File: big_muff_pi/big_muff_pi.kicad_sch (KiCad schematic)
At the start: 77 parts, among them J1 Jack_6.35, J2 Jack_6.35, J3 Conn_01x05, J4 Conn_01x05, J5 Conn_01x05, J7 Conn_01x01_Socket, J8 Conn_01x01_Socket, J9 Barrel_Jack_Switch, P1 big_muff_pi_front_panel, Q1 MMBT5551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

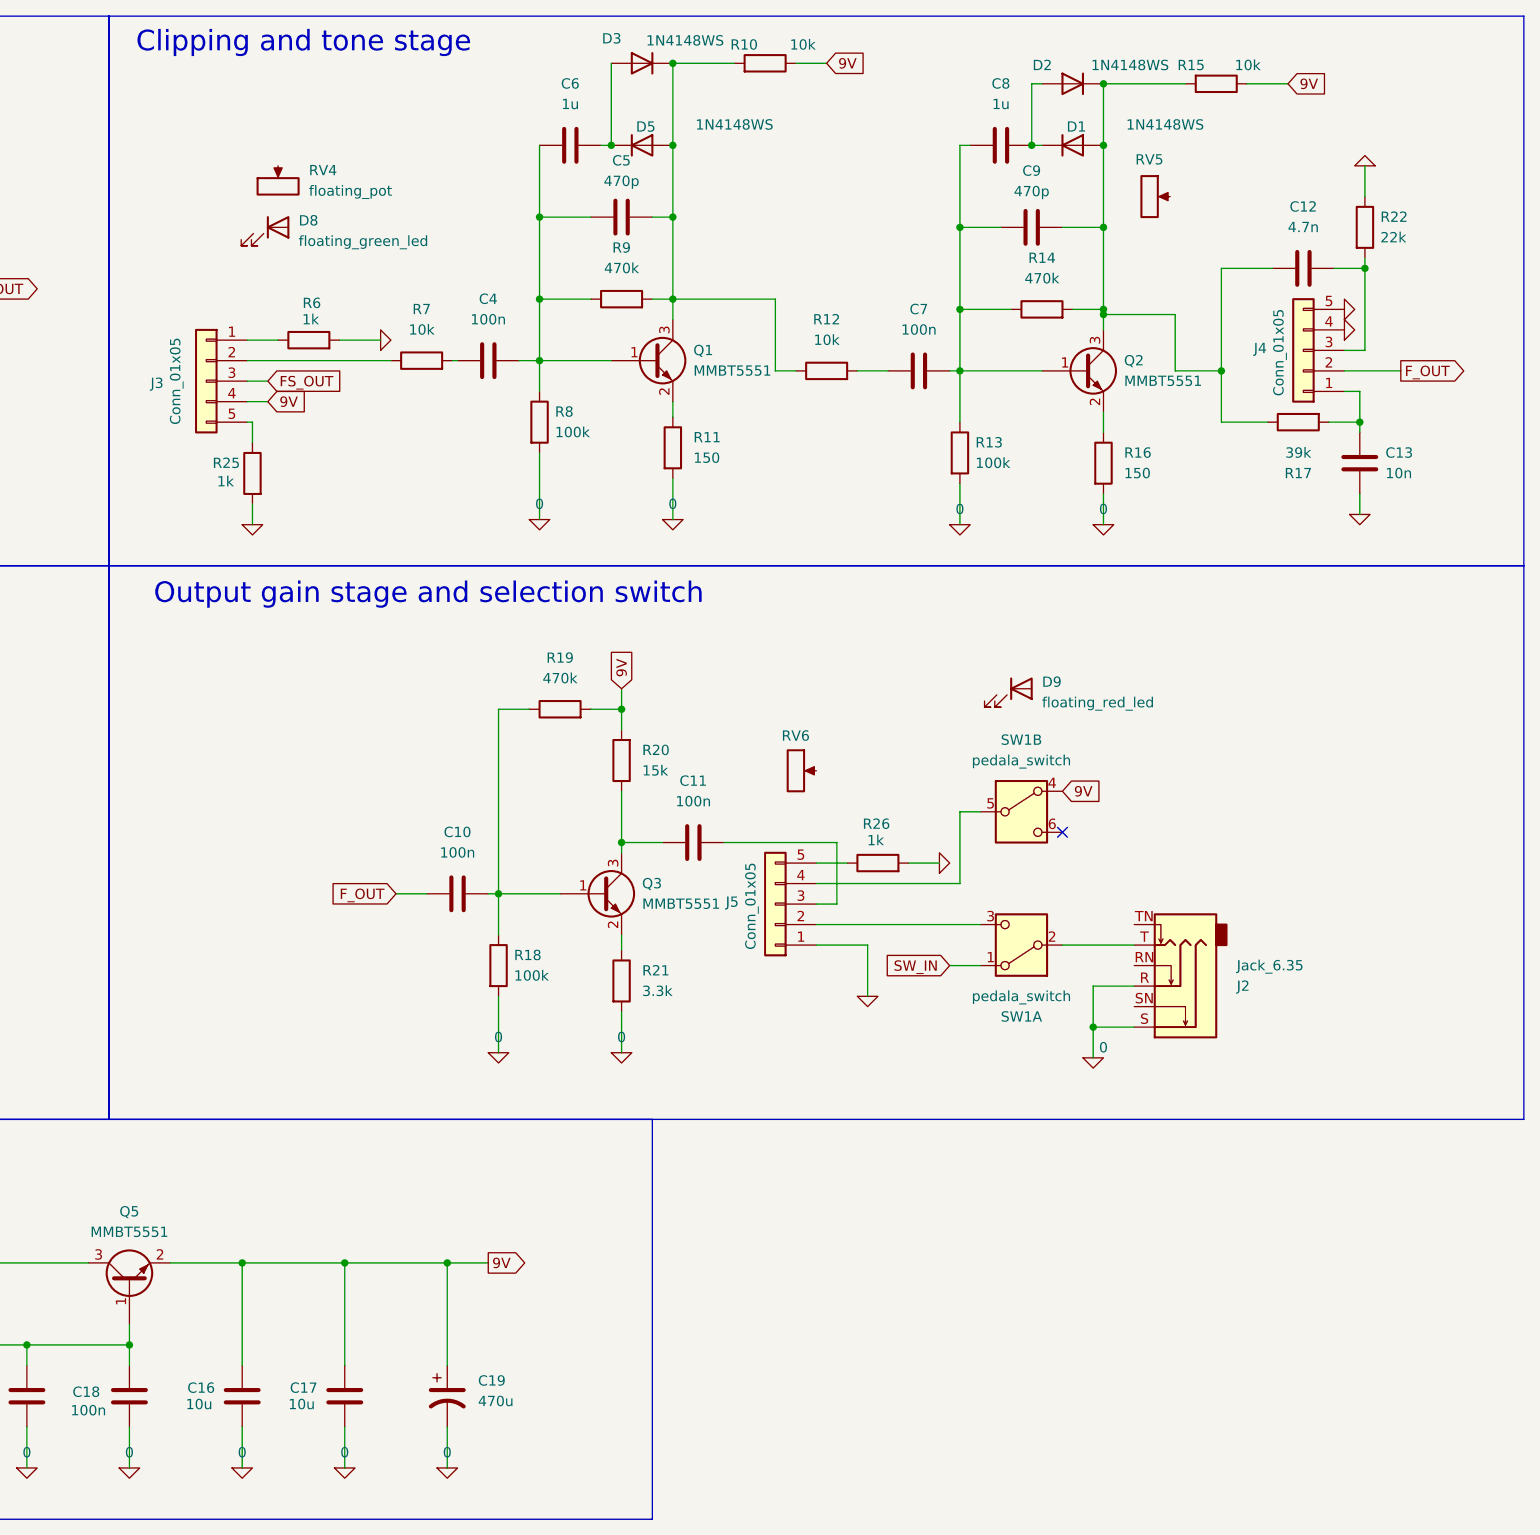
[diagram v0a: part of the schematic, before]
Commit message: Added IDC, added front plate.
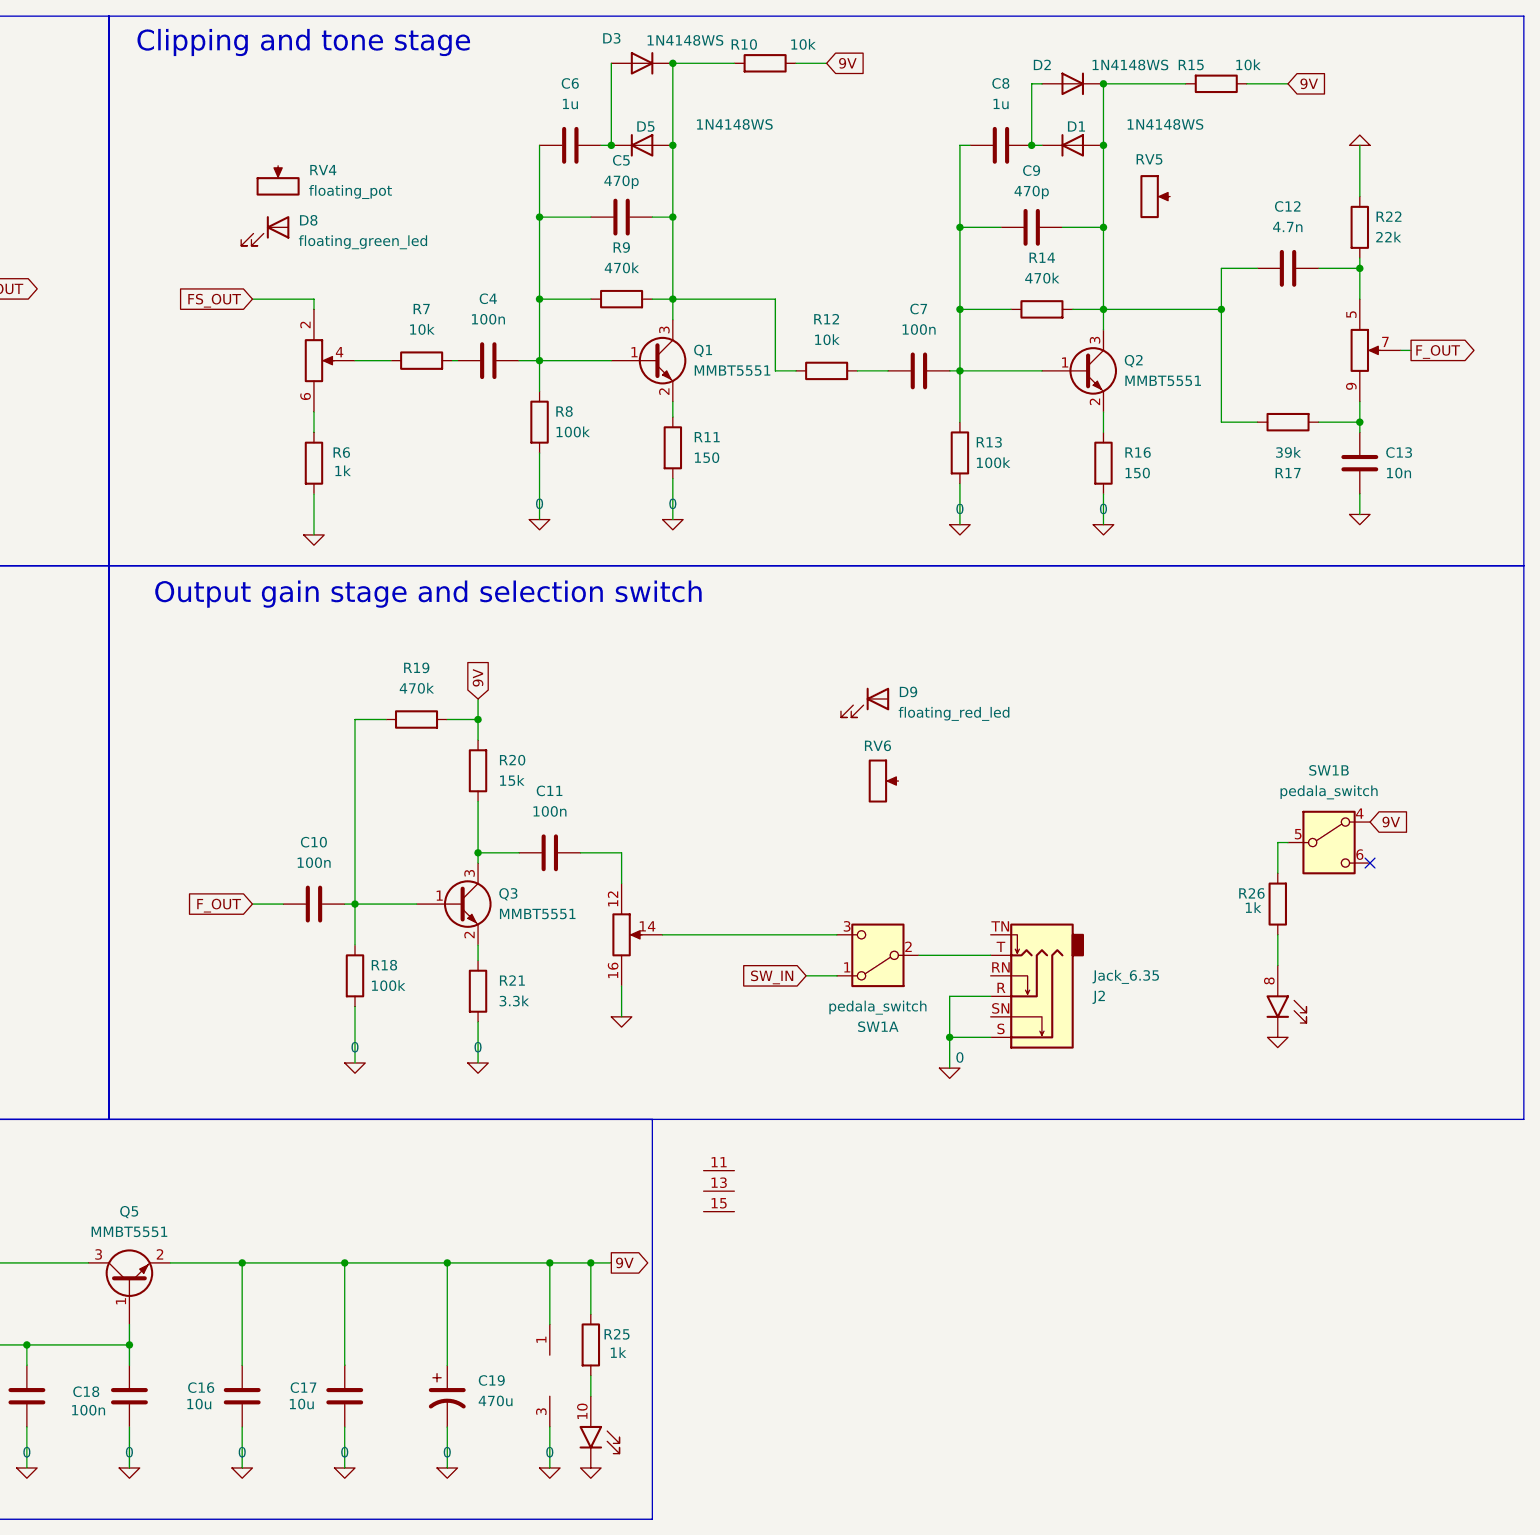
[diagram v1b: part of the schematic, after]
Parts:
- removed J3, J4, J5: Conn_01x05, Connector_JST:JST_EH_B5B-EH-A_1x05_P2.50mm_Vertical, symbol Connector_Generic:Conn_01x05
- added J6: top_panel_connector, Connector_IDC:IDC-Header_2x08_P2.54mm_Vertical, symbol pedale:top_panel_connector
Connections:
- net 0: now also J6.16 (Pin_16), J6.3 (GND); no longer R25.2, R26.2
- net 9V: now also R25.1, J6.1 (VCC)
- net FS_OUT: now also J6.2 (Pin_2)
- net F_OUT: now also J6.7 (Pin_7)
- net at R6.1: now also J6.6 (Pin_6)
- net at R7.1: now also J6.4 (Pin_4)
- net at SW1.5 (B): now also R26.2
- net at C12.2, R22.2: now also J6.5 (Pin_5)
- net at SW1.3 (C): now also J6.14 (Pin_14)
- net at C13.2, R17.2: now also J6.9 (Pin_9)
- net at C11.2: now also J6.12 (Pin_12)
- net at R26.1: now also J6.8 (Pin_8)
- new net: J6.10 (Pin_10), R25.2
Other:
- moved on the sheet: C10, C11, C12, D9, J2, Q3, R17, R18, R19, R20, R21, R22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

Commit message: Added PMOS.
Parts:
- removed D4: 1N4148WS, Diode_SMD:D_SOD-323, symbol Diode:1N4148WS
- added Q6: AO3401A, Package_TO_SOT_SMD:SOT-23, symbol Transistor_FET:AO3401A
- added Q7: MMBT5551, Package_TO_SOT_SMD:SOT-23, symbol Transistor_BJT:BC817
- added R23, R27: 100k, Resistor_SMD:R_0603_1608Metric_Pad0.98x0.95mm_HandSolder, symbol Device:R
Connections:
- net 0: now also Q7.2 (E)
- net REG_IN: now reaches D7.1 (K), Q5.3 (C), R24.2
- net REG_IN: now also Q6.2 (S)
- net BAT+: now reaches BT1.1 (+), J7.1 (Pin_1)
- net BAT+: now also Q6.3 (D), R23.1, R27.1
- net BAT-: now reaches BT1.2 (-), J8.1 (Pin_1), J9.3
- net IN_CONNECT: now reaches J1.SN
- net IN_CONNECT: now also Q7.1 (B), R27.2
- new net: Q6.1 (G), Q7.3 (C), R23.2
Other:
- moved on the sheet: BT1, C14, C16, C17, C18, C19, C20, D7, J7, J8, J9, Q5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
